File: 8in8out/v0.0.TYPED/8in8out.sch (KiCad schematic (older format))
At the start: 61 parts, among them IC1 ATTINY48-A, J1 RJ45, J2 RJ45, J3 CONN_6, K110 G5T-1-12VDC, K120 G5T-1-12VDC, K130 G5T-1-12VDC, K140 G5T-1-12VDC, K150 G5T-1-12VDC, K160 G5T-1-12VDC, K170 G5T-1-12VDC, K180 G5T-1-12VDC, P1 CONN_5, P100 CONN_2, P101 CONN_2, P102 CONN_2, P103 CONN_2, P105 CONN_2, P106 CONN_2, P110 CONN_2, P120 CONN_2, P130 CONN_2, P140 CONN_2, P150 CONN_2, P160 CONN_2, P170 CONN_2, P180 CONN_2, P2 CONN_5, P3 CONN_10X2, P4 CONN_2, U1 7805, U10 OPTO-TRANSISTOR, U2 ULN2803, U20 OPTO-TRANSISTOR, U30 OPTO-TRANSISTOR, U40 OPTO-TRANSISTOR, U50 OPTO-TRANSISTOR, U60 OPTO-TRANSISTOR, U70 OPTO-TRANSISTOR, U80 OPTO-TRANSISTOR

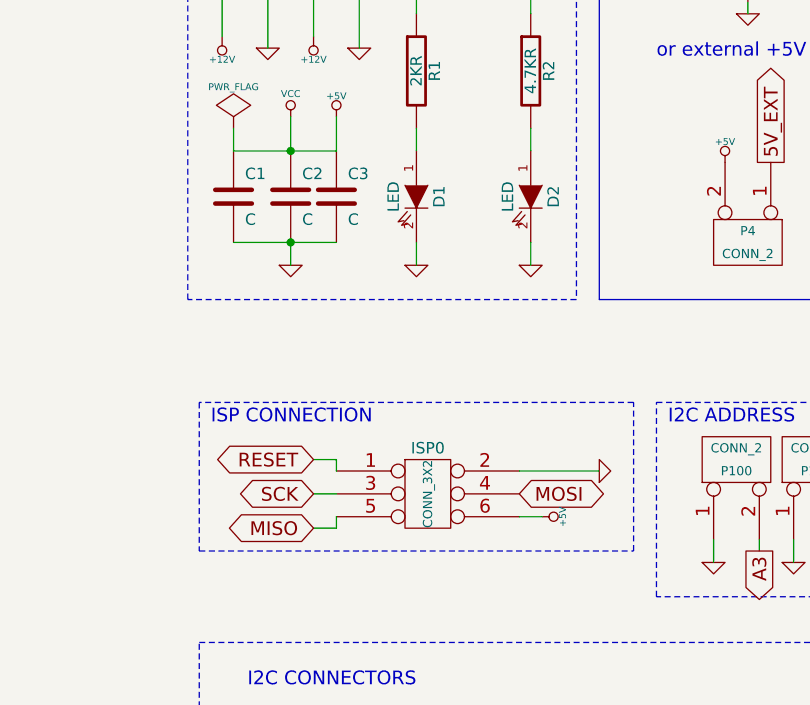
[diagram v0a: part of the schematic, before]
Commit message: correction connecteur ISP
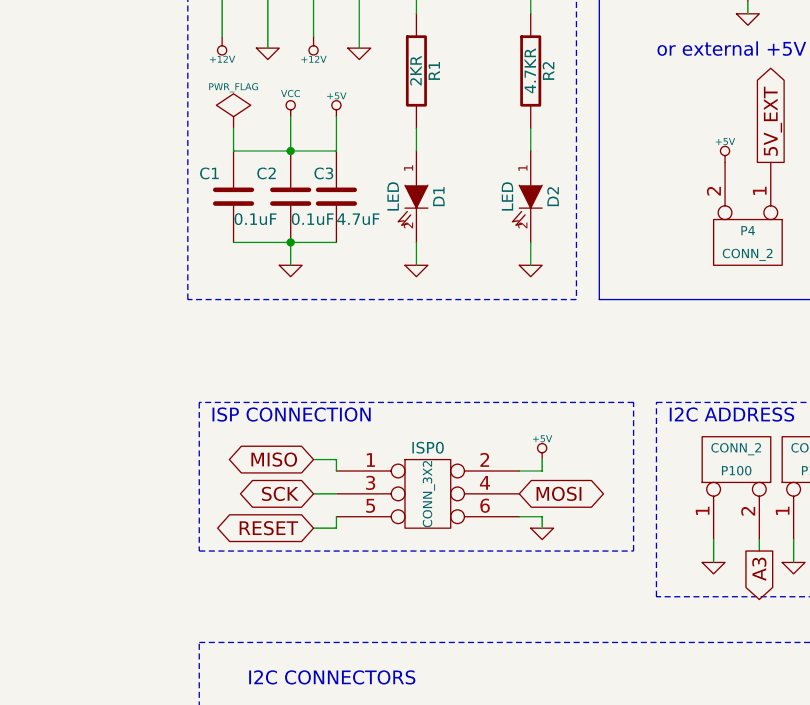
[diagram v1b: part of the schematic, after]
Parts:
- C1, C2: value C -> 0.1uF
- C3: value C -> 4.7uF
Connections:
- net +5V: now also ISP0.2; no longer ISP0.6
- net GND: now also ISP0.6; no longer ISP0.2
- net MISO: now also ISP0.1; no longer ISP0.5
- net RESET: now also ISP0.5; no longer ISP0.1
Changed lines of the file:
@@
-EESchema Schematic File Version 2  date dim. 02 juin 2013 15:29:56 CEST
+EESchema Schematic File Version 2
 LIBS:g5la-1-12vdc
 LIBS:power
@@
 L +5V #PWR03
 U 1 1 50670686
-P 11800 5050
-F 0 "#PWR03" H 11800 5140 20  0001 C CNN
-F 1 "+5V" H 11800 5140 30  0000 C CNN
-F 2 "" H 11800 5050 60  0001 C CNN
-F 3 "" H 11800 5050 60  0001 C CNN
-	1    11800 5050
-	0    1    1    0
+P 11800 4800
+F 0 "#PWR03" H 11800 4890 20  0001 C CNN
+F 1 "+5V" H 11800 4890 30  0000 C CNN
+F 2 "" H 11800 4800 60  0001 C CNN
+F 3 "" H 11800 4800 60  0001 C CNN
+	1    11800 4800
+	1    0    0    -1
 $EndComp
 Text Notes 10350 4650 0    60   ~ 0
@@
 U 1 1 5067601F
 P 10450 3650
-F 0 "C1" H 10500 3750 50  0000 L CNN
-F 1 "C" H 10500 3550 50  0000 L CNN
+F 0 "C1" H 10300 3750 50  0000 L CNN
+F 1 "0.1uF" H 10450 3550 50  0000 L CNN
 F 2 "" H 10450 3650 60  0001 C CNN
 F 3 "" H 10450 3650 60  0001 C CNN
@@
 U 1 1 5067602E
 P 10700 3650
-F 0 "C2" H 10750 3750 50  0000 L CNN
-F 1 "C" H 10750 3550 50  0000 L CNN
+F 0 "C2" H 10550 3750 50  0000 L CNN
+F 1 "0.1uF" H 10700 3550 50  0000 L CNN
 F 2 "" H 10700 3650 60  0001 C CNN
 F 3 "" H 10700 3650 60  0001 C CNN
@@
 L GND #PWR025
 U 1 1 5135D759
-P 12050 4850
-F 0 "#PWR025" H 12050 4850 30  0001 C CNN
-F 1 "GND" H 12050 4780 30  0001 C CNN
-F 2 "" H 12050 4850 60  0001 C CNN
-F 3 "" H 12050 4850 60  0001 C CNN
-	1    12050 4850
-	0    -1   -1   0
+P 11800 5100
+F 0 "#PWR025" H 11800 5100 30  0001 C CNN
+F 1 "GND" H 11800 5030 30  0001 C CNN
+F 2 "" H 11800 5100 60  0001 C CNN
+F 3 "" H 11800 5100 60  0001 C CNN
+	1    11800 5100
+	1    0    0    -1
 $EndComp
 $Comp
@@
 RESET
 Connection ~ 13700 10550
-Text GLabel 10800 4800 0    60   BiDi ~ 0
+Text GLabel 10800 5100 0    60   BiDi ~ 0
 RESET
 Text GLabel 10800 4950 0    60   BiDi ~ 0
 SCK
-Text GLabel 10800 5100 0    60   BiDi ~ 0
+Text GLabel 10800 4800 0    60   BiDi ~ 0
 MISO
 Text GLabel 11700 4950 2    60   BiDi ~ 0
@@
 Wire Wire Line
 	10900 5100 10900 5050
-Wire Wire Line
-	11700 4850 12050 4850
 $Comp
 L CONN_5 P1
@@
 U 1 1 51AB4C03
 P 10900 3650
-F 0 "C3" H 10950 3750 50  0000 L CNN
-F 1 "C" H 10950 3550 50  0000 L CNN
+F 0 "C3" H 10800 3750 50  0000 L CNN
+F 1 "4.7uF" H 10900 3550 50  0000 L CNN
 F 2 "" H 10900 3650 60  0001 C CNN
 F 3 "" H 10900 3650 60  0001 C CNN
@@
 Wire Wire Line
 	10450 3450 10900 3450
+Wire Wire Line
+	11800 5050 11800 5100
+Wire Wire Line
+	11700 4850 11800 4850
+Wire Wire Line
+	11800 4850 11800 4800
 $EndSCHEMATC

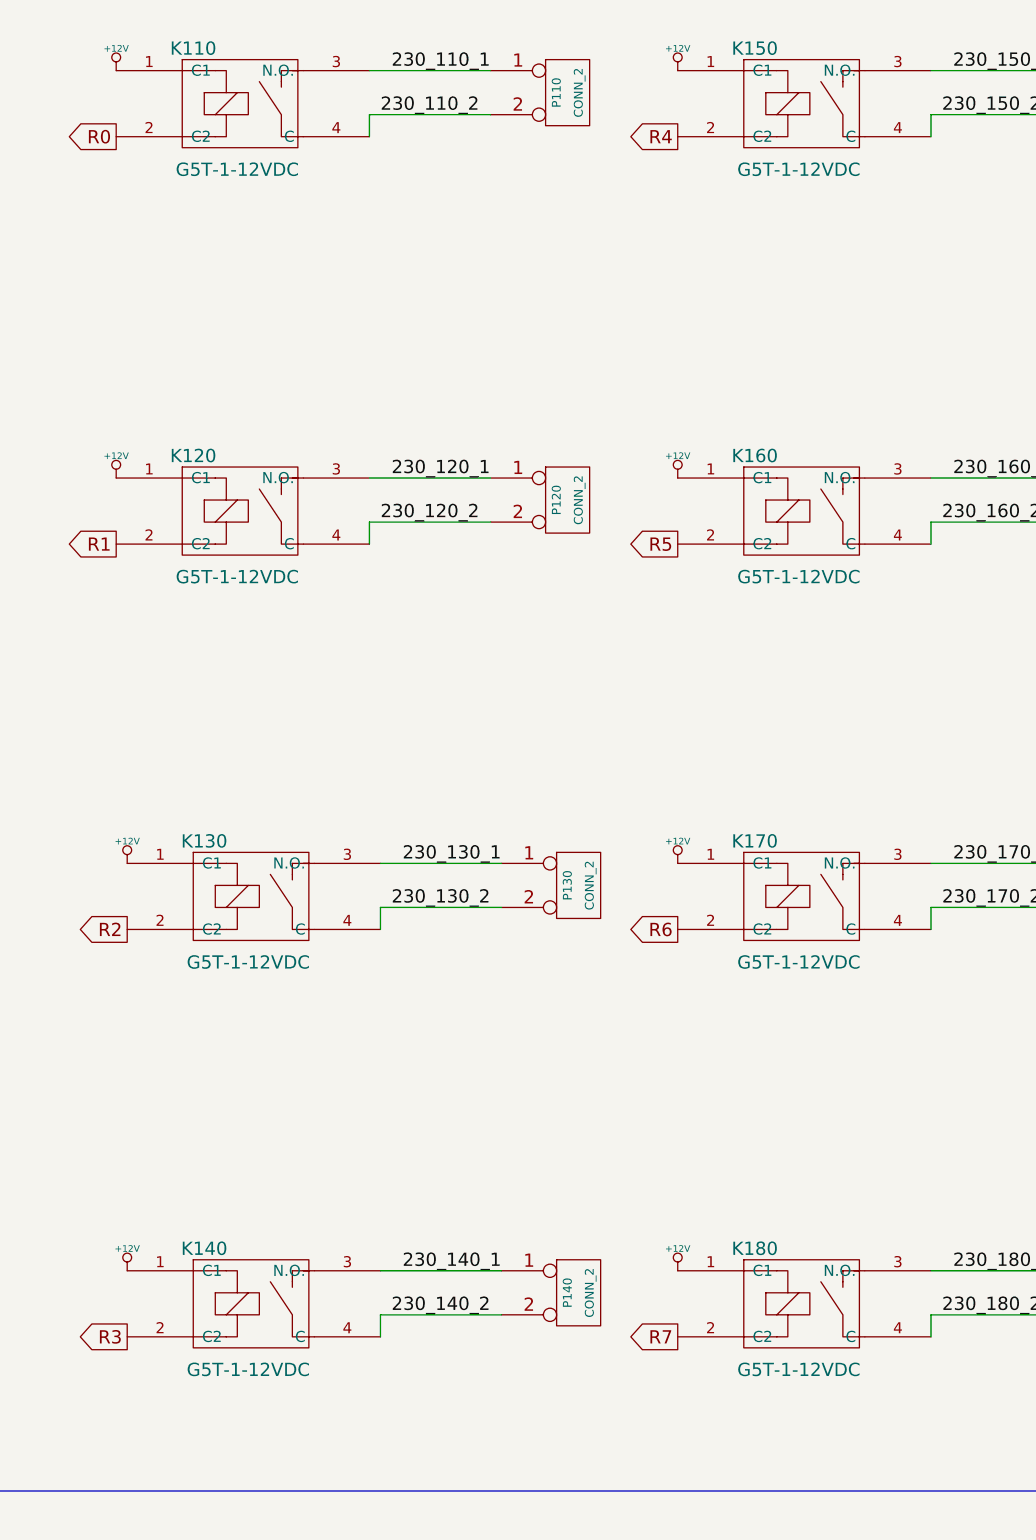
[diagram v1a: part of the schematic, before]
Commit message: reprise connecteur correction mask back connecteur 230v serigraphie complete double piste relais cot? puissance verification routage generation gerber bon pour fab ?
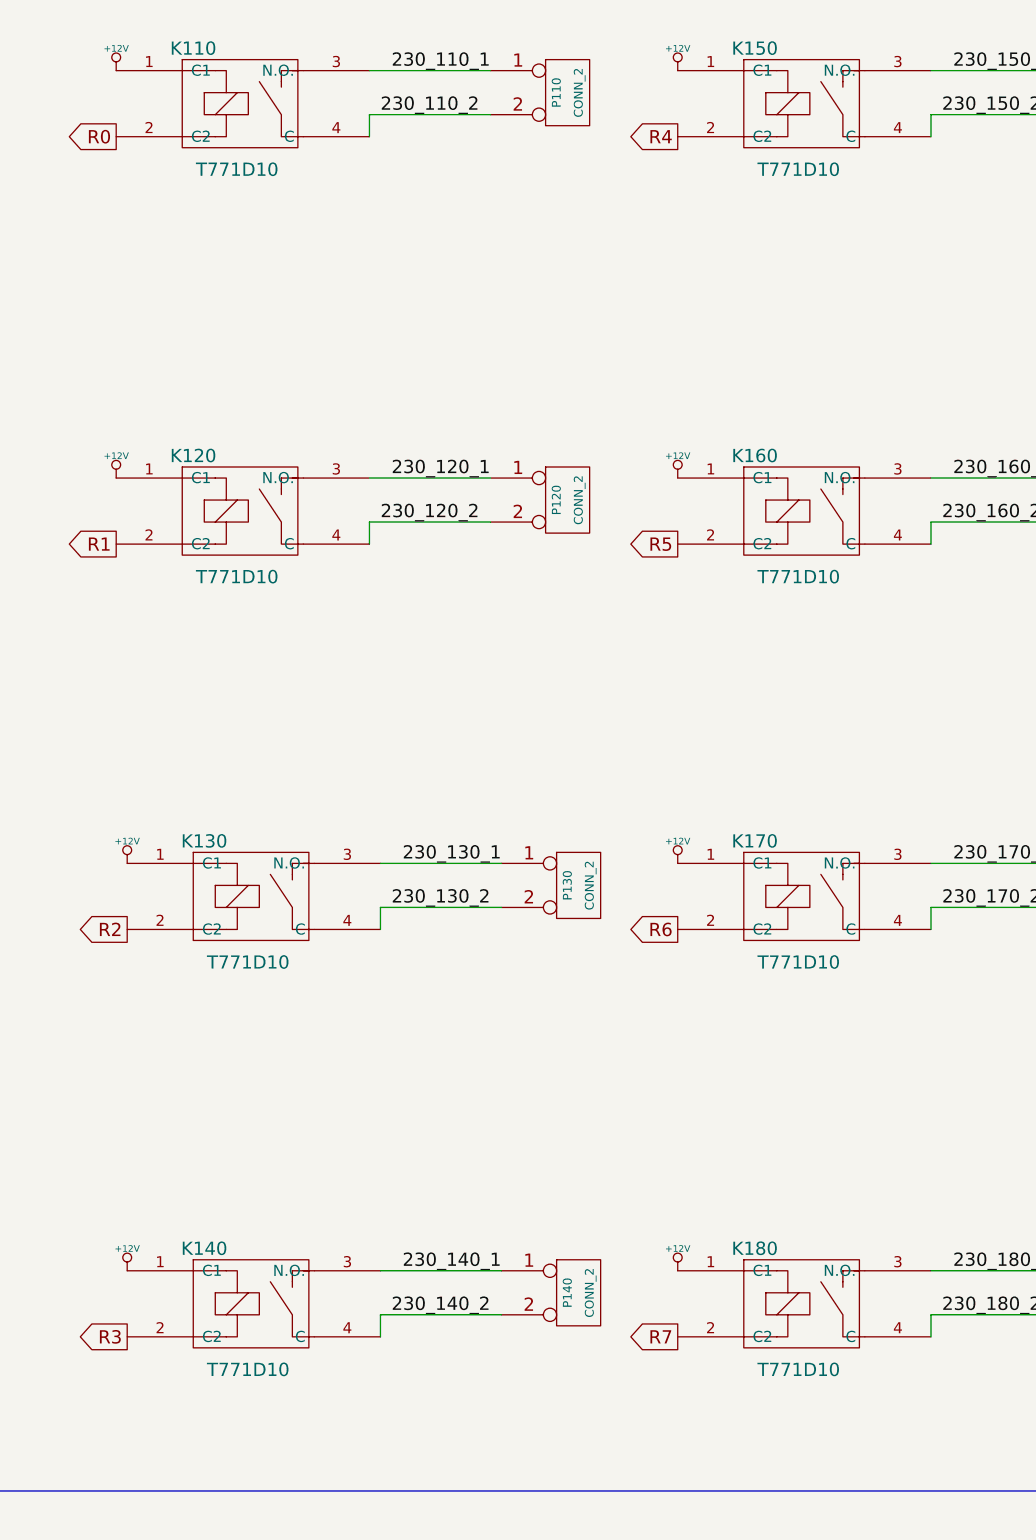
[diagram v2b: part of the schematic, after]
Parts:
- K110, K120, K130, K140, K150, K160, K170, K180: value G5T-1-12VDC -> T771D10
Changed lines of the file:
@@
 P 16000 4650
 F 0 "K110" H 15850 4900 60  0000 C CNN
-F 1 "G5T-1-12VDC" H 16050 4350 60  0000 C CNN
+F 1 "T771D10" H 16050 4350 60  0000 C CNN
 F 2 "G5T-1-12VDC" H 16000 4650 60  0001 C CNN
 F 3 "" H 16000 4650 60  0001 C CNN
@@
 P 16000 6500
 F 0 "K120" H 15850 6750 60  0000 C CNN
-F 1 "G5T-1-12VDC" H 16050 6200 60  0000 C CNN
+F 1 "T771D10" H 16050 6200 60  0000 C CNN
 F 2 "G5T-1-12VDC" H 16000 6500 60  0001 C CNN
 F 3 "" H 16000 6500 60  0001 C CNN
@@
 P 16050 8250
 F 0 "K130" H 15900 8500 60  0000 C CNN
-F 1 "G5T-1-12VDC" H 16100 7950 60  0000 C CNN
+F 1 "T771D10" H 16100 7950 60  0000 C CNN
 F 2 "G5T-1-12VDC" H 16050 8250 60  0001 C CNN
 F 3 "" H 16050 8250 60  0001 C CNN
@@
 P 16050 10100
 F 0 "K140" H 15900 10350 60  0000 C CNN
-F 1 "G5T-1-12VDC" H 16100 9800 60  0000 C CNN
+F 1 "T771D10" H 16100 9800 60  0000 C CNN
 F 2 "G5T-1-12VDC" H 16050 10100 60  0001 C CNN
 F 3 "" H 16050 10100 60  0001 C CNN
@@
 P 18550 4650
 F 0 "K150" H 18400 4900 60  0000 C CNN
-F 1 "G5T-1-12VDC" H 18600 4350 60  0000 C CNN
+F 1 "T771D10" H 18600 4350 60  0000 C CNN
 F 2 "G5T-1-12VDC" H 18550 4650 60  0001 C CNN
 F 3 "" H 18550 4650 60  0001 C CNN
@@
 P 18550 6500
 F 0 "K160" H 18400 6750 60  0000 C CNN
-F 1 "G5T-1-12VDC" H 18600 6200 60  0000 C CNN
+F 1 "T771D10" H 18600 6200 60  0000 C CNN
 F 2 "G5T-1-12VDC" H 18550 6500 60  0001 C CNN
 F 3 "" H 18550 6500 60  0001 C CNN
@@
 P 18550 8250
 F 0 "K170" H 18400 8500 60  0000 C CNN
-F 1 "G5T-1-12VDC" H 18600 7950 60  0000 C CNN
+F 1 "T771D10" H 18600 7950 60  0000 C CNN
 F 2 "G5T-1-12VDC" H 18550 8250 60  0001 C CNN
 F 3 "" H 18550 8250 60  0001 C CNN
@@
 P 18550 10100
 F 0 "K180" H 18400 10350 60  0000 C CNN
-F 1 "G5T-1-12VDC" H 18600 9800 60  0000 C CNN
+F 1 "T771D10" H 18600 9800 60  0000 C CNN
 F 2 "G5T-1-12VDC" H 18550 10100 60  0001 C CNN
 F 3 "" H 18550 10100 60  0001 C CNN
